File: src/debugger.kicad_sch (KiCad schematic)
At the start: 30 parts, among them J1 SM03B-SRSS-TB, J6 USB_C_Receptacle_USB2.0_16P, U7 RP2040, U8 W25Q128JVS, U9 NCP1117-1.5_SOT223, Y1 ABM8-272-T3

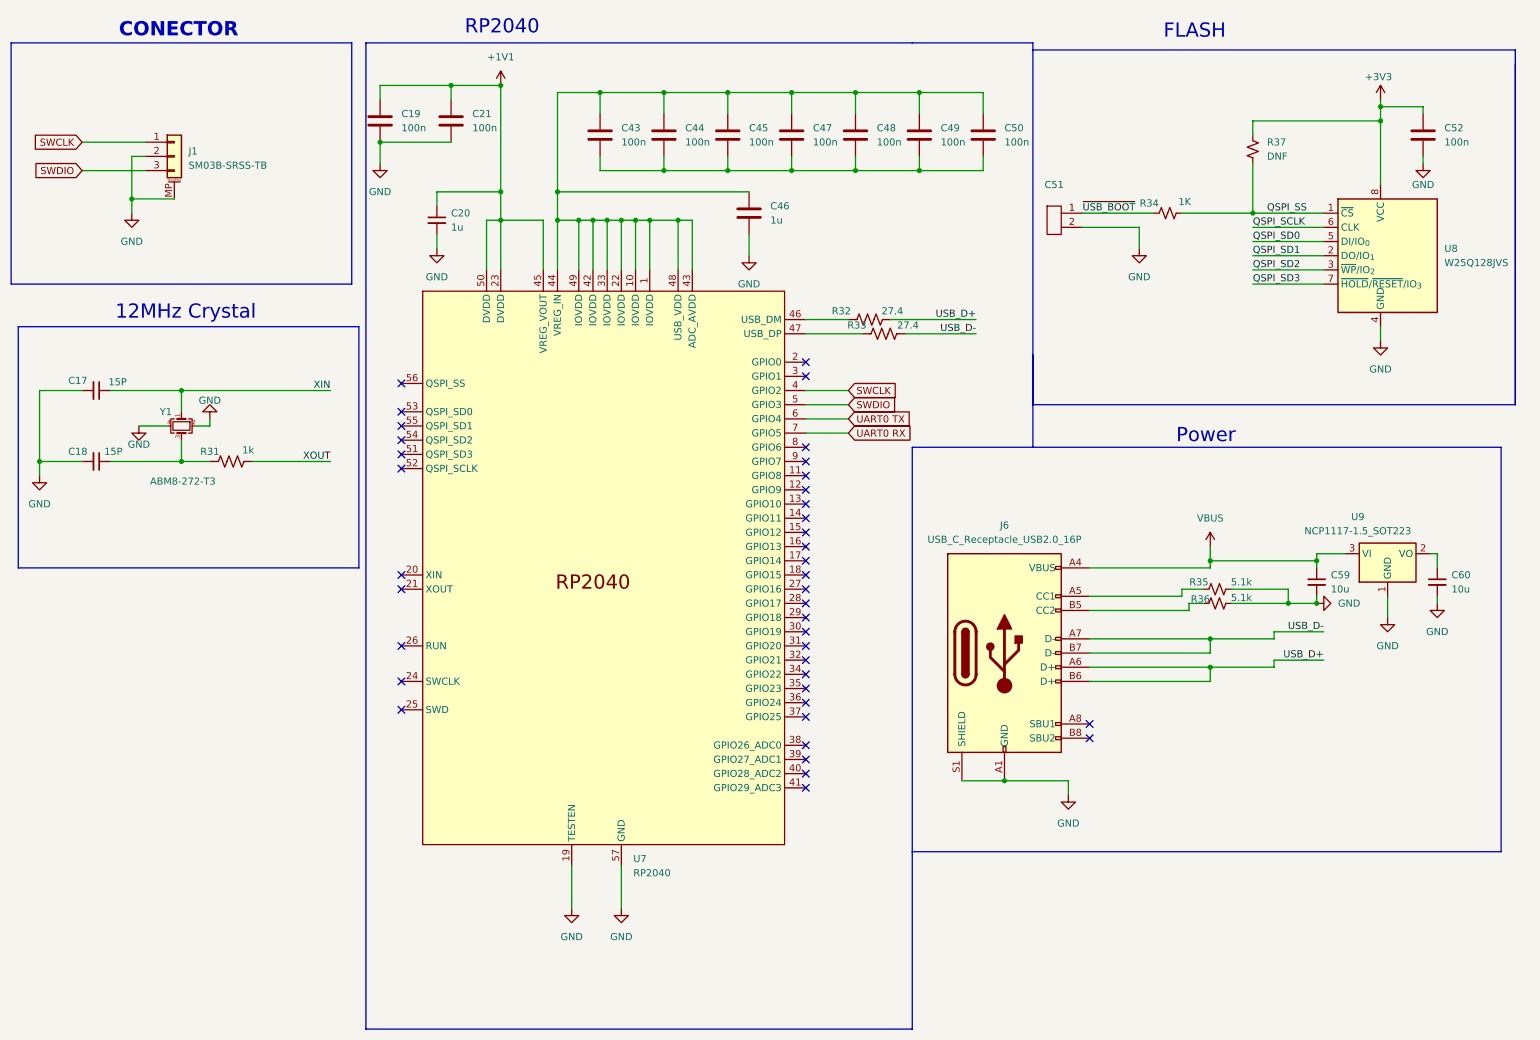
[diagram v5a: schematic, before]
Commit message: Subconjuntos organizados na PCI
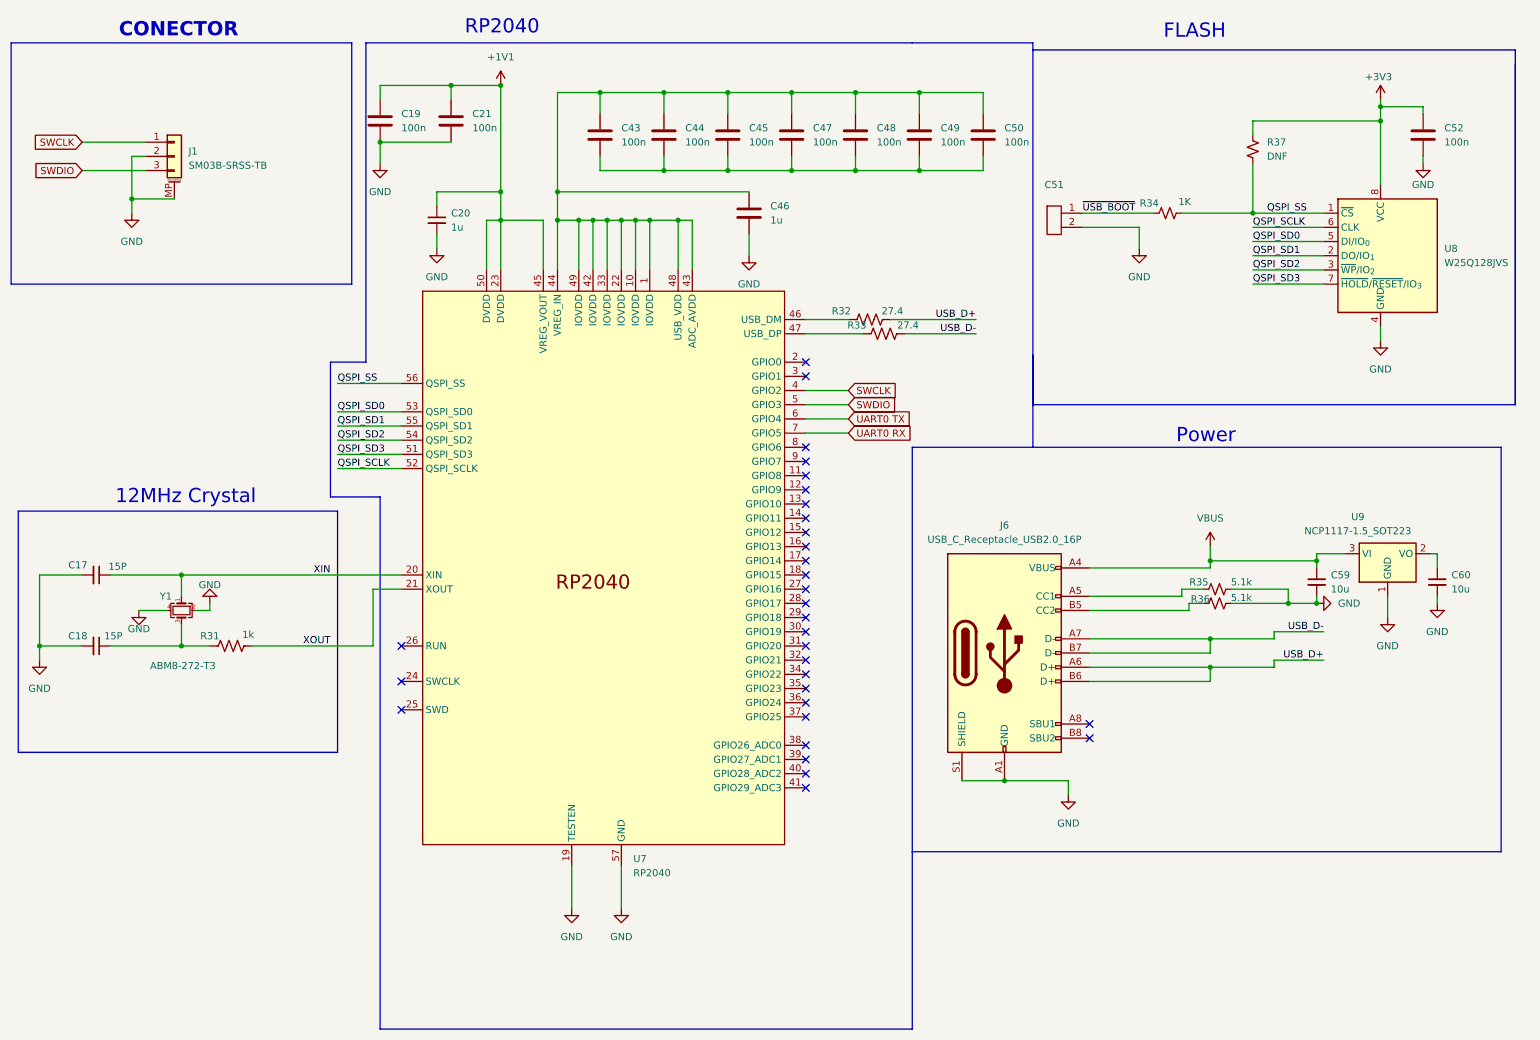
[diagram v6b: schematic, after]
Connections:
- net QSPI_SCLK: now also U7.52 (QSPI_SCLK)
- net QSPI_SD0: now also U7.53 (QSPI_SD0)
- net QSPI_SD1: now also U7.55 (QSPI_SD1)
- net QSPI_SD2: now also U7.54 (QSPI_SD2)
- net QSPI_SD3: now also U7.51 (QSPI_SD3)
- net QSPI_SS: now also U7.56 (QSPI_SS)
- net XIN: now also U7.20 (XIN)
- net XOUT: now also U7.21 (XOUT)
- no-connect marks 39 -> 31
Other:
- moved on the sheet: C17, C18, R31, Y1
